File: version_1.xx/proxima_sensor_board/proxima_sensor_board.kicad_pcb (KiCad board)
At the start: 2 copper layers, 15 x 10 mm, 16 parts, among them J1 Conn_01x03, Q1 Q_NPN_EBC, U1 TSOP32156, U2 NE555D

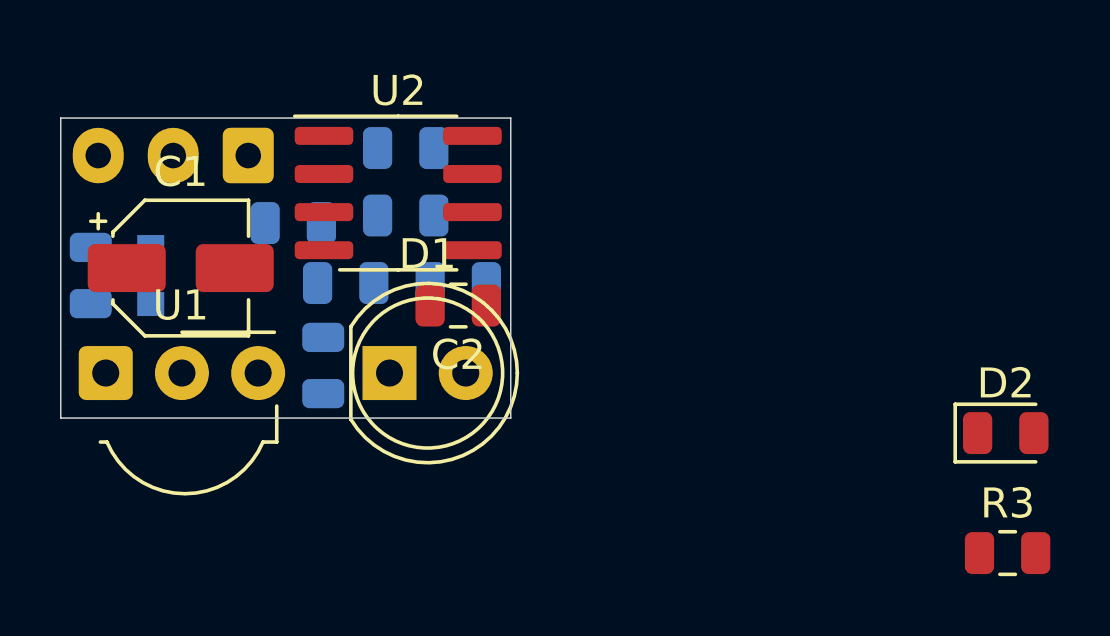
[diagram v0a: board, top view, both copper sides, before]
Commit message: Delete unnecessary components
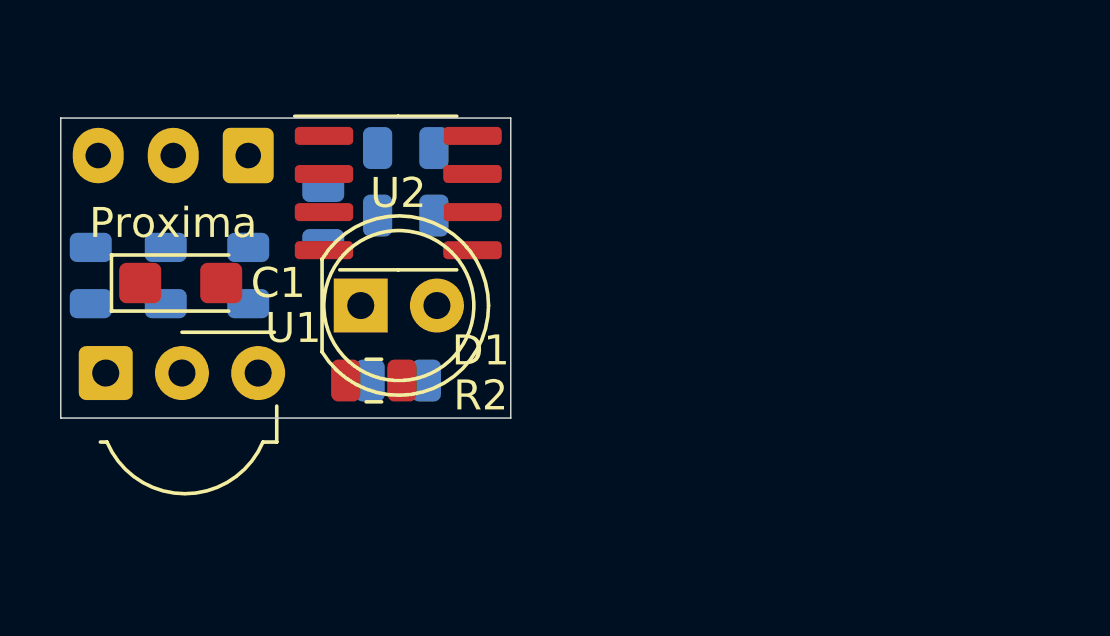
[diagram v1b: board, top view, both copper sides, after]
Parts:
- removed Q1: Q_NPN_EBC, Package_TO_SOT_SMD:SOT-23
- removed the R4 at (169.2, 77.5)
- removed the R5 at (174.8, 79.5)
- C1: footprint Capacitor_SMD:CP_Elec_4x5.4 -> Capacitor_Tantalum_SMD:CP_EIA-3216-10_Kemet-I
- C2, D2: moved to B.Cu
- R2: value 82 -> 47; moved to F.Cu
- R3: renamed from R6; value 1k -> 1k5
- R5: renamed from R3; moved to B.Cu
- moved D2 28.5 mm to (165.0, 79.2), turned to 90 degrees
- moved R5 26.9 mm to (167.8, 79.2), turned to 90 degrees
- moved C2 3.20 mm to (172.8, 82.8)
- moved D1 2.45 mm to (171.5, 80.2)
- moved R3 2.37 mm to (170.2, 77.2), turned to 90 degrees
- moved R2 1.76 mm to (171.9, 82.8), turned to 180 degrees
- moved C1 0.50 mm to (165.5, 79.5)
- renumbered R7 to R4
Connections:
- D1 pad 2: VCC -> SQUARE_WAVE_SIGNAL
- R2 pad 2: Net-(Q1-Pad3) -> GND
- R3 pad 1: Net-(R5-Pad2) -> VCC
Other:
- board text added: "E. Możdżeń"
- board text added: "Proxima"

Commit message: Smaller connector and version number
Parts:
- J1: footprint Connector_Molex:Molex_SPOX_5267-03A_1x03_P2.50mm_Vertical -> Connector_PinHeader_2.54mm:PinHeader_1x03_P2.54mm_Vertical
- moved J1 0.35 mm to (168.0, 75.5), turned to 90 degrees
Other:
- board text added: "V1.0"

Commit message: Routes ready
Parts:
- moved D1 2.50 mm to (174.0, 80.3), turned to 180 degrees
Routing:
- net VCC: track 0.00 -> 23.7 mm, vias 0 -> 2
- net GND: track 0.00 -> 19.5 mm, vias 0 -> 1
- net OUTPUT_INVERTED: track 0.00 -> 14.1 mm, vias 0 -> 1
- net Net-(C3-Pad1): track 0.00 -> 9.92 mm, vias 0 -> 2
- net Net-(R3-Pad2): track 0.00 -> 6.03 mm, vias 0 -> 1
- net Net-(C2-Pad1): track 0.00 -> 6.00 mm, vias 0 -> 1
- net Net-(C1-Pad1): track 0.00 -> 5.52 mm, vias 0 -> 1
- net SQUARE_WAVE_SIGNAL: track 0.00 -> 4.83 mm
- net Net-(D1-Pad1): track 0.00 -> 2.87 mm
- net Net-(D2-Pad1): track 0.00 -> 2.75 mm
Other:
- outline, holes or cut-outs redrawn

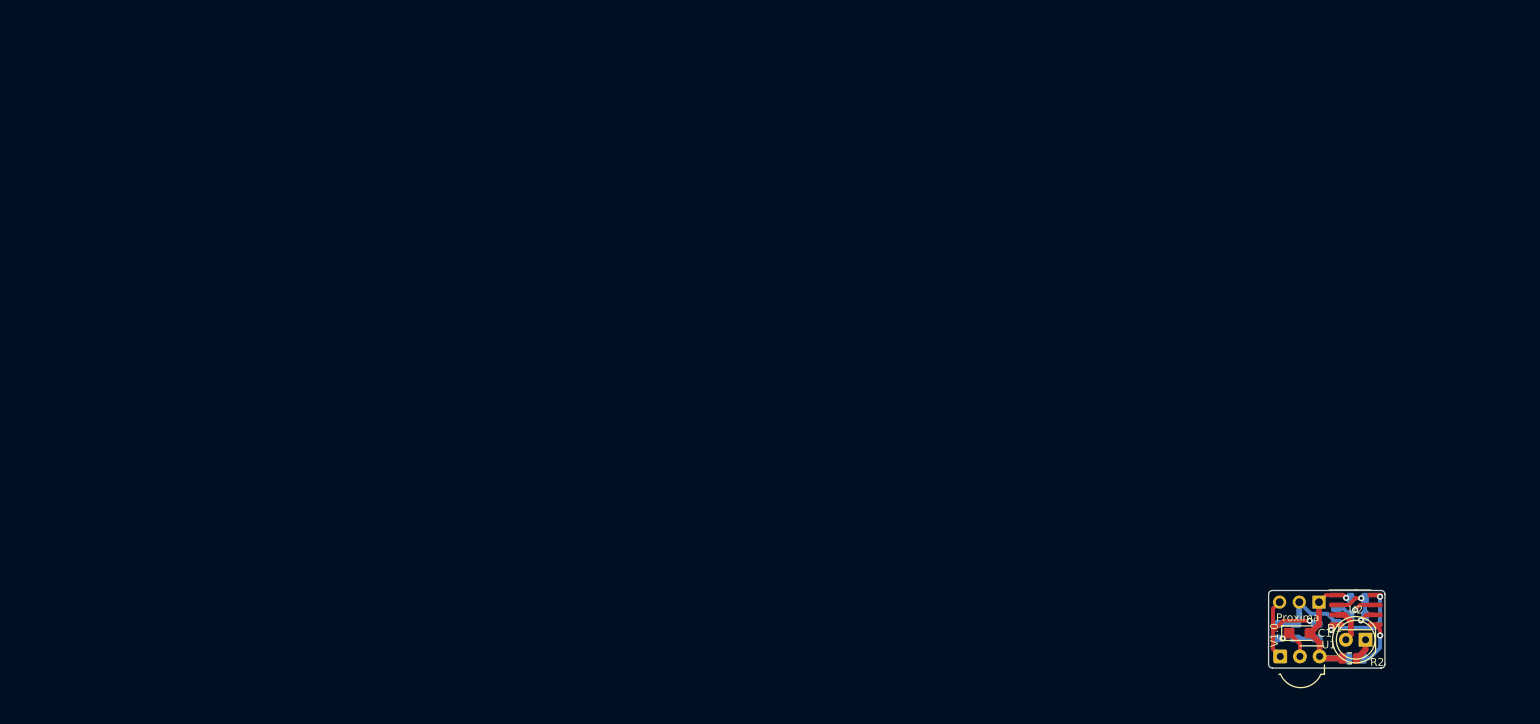
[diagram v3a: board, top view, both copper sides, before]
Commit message: Panelize board and gerbers
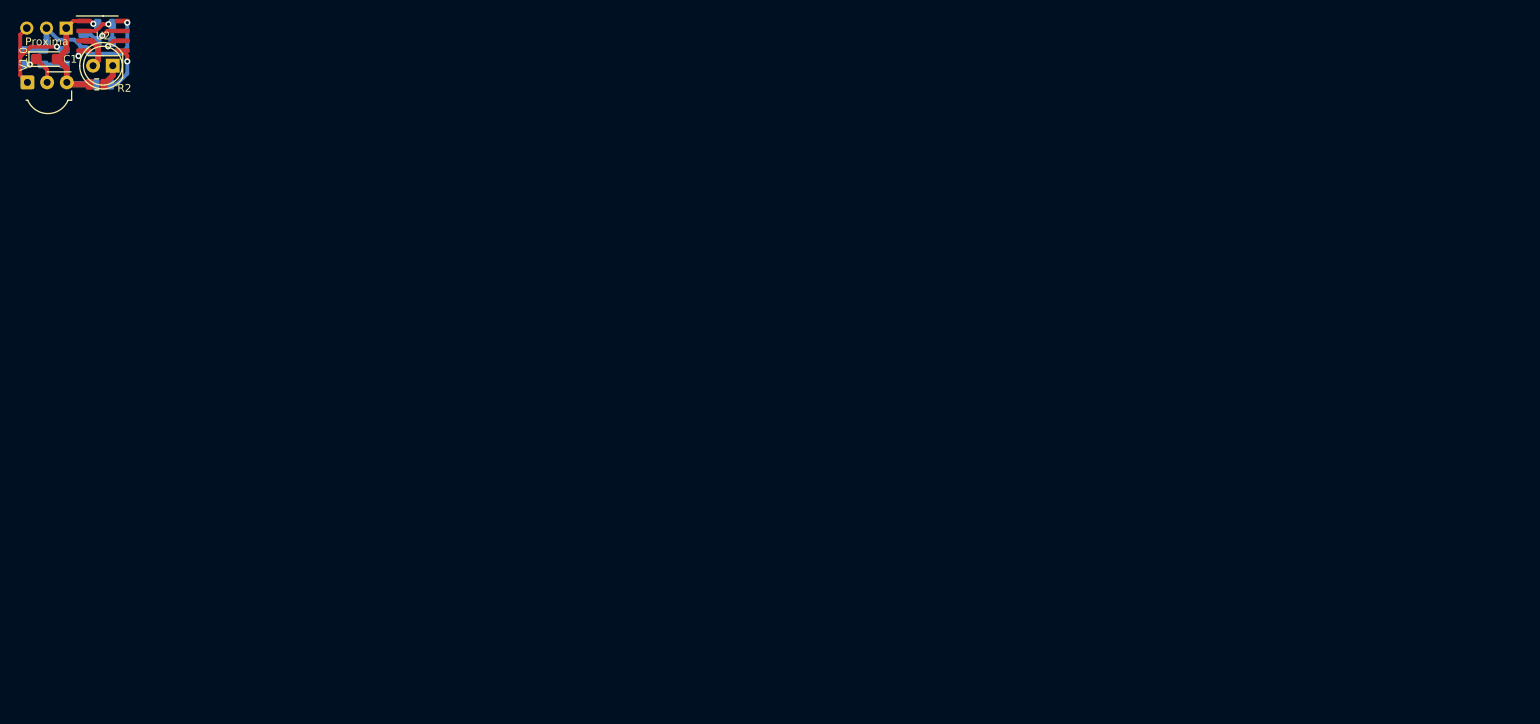
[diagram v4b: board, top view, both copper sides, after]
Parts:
- C1: footprint Capacitor_Tantalum_SMD:CP_EIA-3216-10_Kemet-I -> Capacitor_Tantalum_SMD:CP_EIA-3216-18_Kemet-A
- moved C1 177.6 mm to (4.00, 5.50)
- moved C2 177.6 mm to (11.2, 8.75)
- moved C3 177.6 mm to (11.5, 1.00)
- moved D1 177.6 mm to (12.5, 6.35)
- moved D2 177.6 mm to (3.50, 5.25)
- moved J1 177.6 mm to (6.50, 1.50)
- moved R1 177.6 mm to (1.00, 5.25)
- moved R2 177.6 mm to (10.4, 8.75)
- moved R3 177.6 mm to (8.75, 3.25)
- moved R4 177.6 mm to (11.5, 3.25)
- moved R5 177.6 mm to (6.25, 5.25)
- moved U1 177.6 mm to (1.50, 8.50)
- moved U2 177.6 mm to (11.2, 2.50)
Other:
- board outline removed
